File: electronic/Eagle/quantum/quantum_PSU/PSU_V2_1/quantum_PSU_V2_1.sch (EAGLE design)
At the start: 37 parts, among them J1 90814-0204, J2 90814-0204, J3 PF0030_PC, U1 7815, U2 7812, U3 7915, U4 7805, U5 LD1117AV33

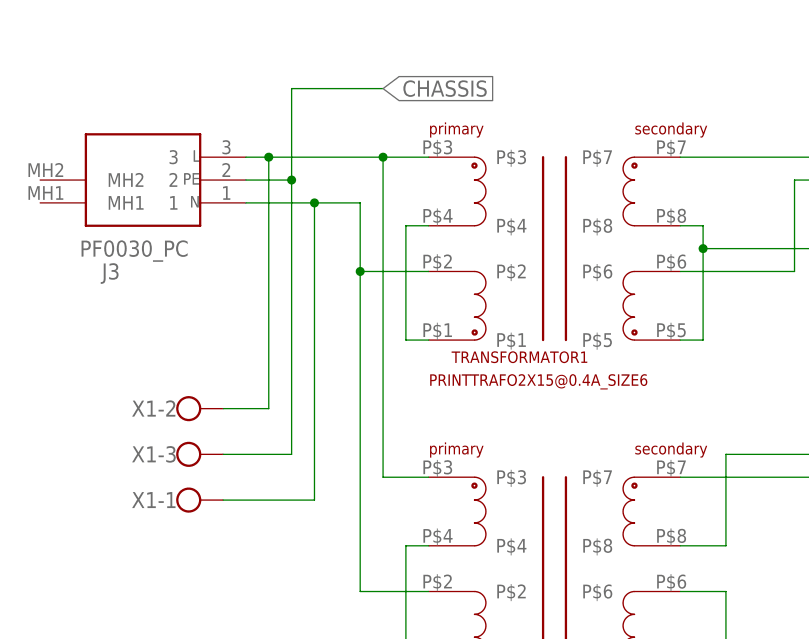
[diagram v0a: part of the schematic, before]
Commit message: several mockups and changes during debugging AnalougeEngine_V5_0. Implemented DSP functionality + rudimental FFT function
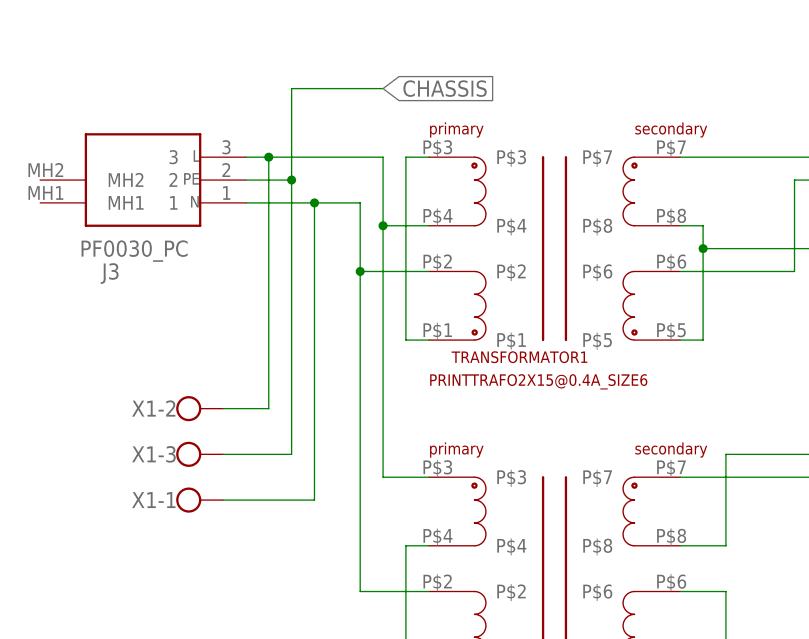
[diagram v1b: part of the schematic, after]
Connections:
- net N$4: now also TRANSFORMATOR1.P$3; no longer TRANSFORMATOR1.P$4
- net N$8: now also TRANSFORMATOR1.P$4; no longer TRANSFORMATOR1.P$3
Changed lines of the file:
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@@
 <layer number="56" name="wert" color="7" fill="1" visible="no" active="no"/>
 <layer number="57" name="tCAD" color="7" fill="1" visible="no" active="no"/>
+<layer number="59" name="tCarbon" color="7" fill="1" visible="no" active="no"/>
+<layer number="60" name="bCarbon" color="7" fill="1" visible="no" active="no"/>
 <layer number="88" name="SimResults" color="9" fill="1" visible="yes" active="yes"/>
 <layer number="89" name="SimProbes" color="9" fill="1" visible="yes" active="yes"/>
@@
 <layer number="112" name="tSilk" color="7" fill="1" visible="no" active="yes"/>
 <layer number="113" name="ReferenceLS" color="7" fill="1" visible="no" active="no"/>
+<layer number="114" name="Badge_Outline" color="11" fill="1" visible="no" active="no"/>
+<layer number="115" name="ReferenceISLANDS" color="7" fill="1" visible="yes" active="yes"/>
 <layer number="116" name="Patch_BOT" color="7" fill="1" visible="yes" active="yes"/>
 <layer number="118" name="Rect_Pads" color="7" fill="1" visible="no" active="no"/>
@@
 <layer number="127" name="_tValues" color="7" fill="1" visible="no" active="yes"/>
 <layer number="128" name="_bValues" color="7" fill="1" visible="no" active="yes"/>
+<layer number="129" name="Mask" color="7" fill="1" visible="yes" active="yes"/>
 <layer number="131" name="tAdjust" color="7" fill="1" visible="no" active="yes"/>
 <layer number="132" name="bAdjust" color="7" fill="1" visible="no" active="yes"/>
@@
 <layer number="223" name="223bmp" color="7" fill="1" visible="yes" active="yes"/>
 <layer number="224" name="224bmp" color="7" fill="1" visible="yes" active="yes"/>
+<layer number="225" name="225bmp" color="7" fill="1" visible="yes" active="yes"/>
+<layer number="226" name="226bmp" color="7" fill="1" visible="yes" active="yes"/>
+<layer number="227" name="227bmp" color="7" fill="1" visible="yes" active="yes"/>
+<layer number="228" name="228bmp" color="7" fill="1" visible="yes" active="yes"/>
+<layer number="229" name="229bmp" color="7" fill="1" visible="yes" active="yes"/>
+<layer number="230" name="230bmp" color="7" fill="1" visible="yes" active="yes"/>
 <layer number="231" name="Eagle3D_PG1" color="7" fill="1" visible="no" active="no"/>
 <layer number="232" name="Eagle3D_PG2" color="7" fill="1" visible="no" active="no"/>
@@
 <layer number="251" name="SMDround" color="7" fill="1" visible="yes" active="yes"/>
 <layer number="254" name="OrgLBR" color="7" fill="1" visible="yes" active="yes"/>
+<layer number="255" name="routoute" color="7" fill="1" visible="yes" active="yes"/>
 </layers>
 <schematic xreflabel="%F%N/%S.%C%R" xrefpart="/%S.%C%R">
@@
 <part name="C3" library="passive components" library_urn="urn:adsk.eagle:library:16365137" deviceset="CAPACITOR_ELECTROLYTIC" device="_16MM-THT" package3d_urn="urn:adsk.eagle:package:1899458/5" value="4700 uF/25 V"/>
 <part name="BR2" library="passive components" library_urn="urn:adsk.eagle:library:16365137" deviceset="BRIDGE_RECTIFIER" device="" package3d_urn="urn:adsk.eagle:package:16388481/3"/>
-<part name="J1" library="electro_mechanical" library_urn="urn:adsk.eagle:library:16388331" deviceset="90814-0204" device="" package3d_urn="urn:adsk.eagle:package:16762552/3"/>
-<part name="J2" library="electro_mechanical" library_urn="urn:adsk.eagle:library:16388331" deviceset="90814-0204" device="" package3d_urn="urn:adsk.eagle:package:16762552/3"/>
+<part name="J1" library="electro_mechanical" library_urn="urn:adsk.eagle:library:16388331" deviceset="90814-0204" device="" package3d_urn="urn:adsk.eagle:package:16762552/4"/>
+<part name="J2" library="electro_mechanical" library_urn="urn:adsk.eagle:library:16388331" deviceset="90814-0204" device="" package3d_urn="urn:adsk.eagle:package:16762552/4"/>
 <part name="J3" library="electro_mechanical" library_urn="urn:adsk.eagle:library:16388331" deviceset="PF0030_PC" device="" package3d_urn="urn:adsk.eagle:package:16991597/2"/>
 <part name="U4" library="passive components" library_urn="urn:adsk.eagle:library:16365137" deviceset="78**" device="_THT" package3d_urn="urn:adsk.eagle:package:1899455/2" value="7805"/>
@@
 <net name="N$8" class="0">
 <segment>
-<pinref part="TRANSFORMATOR1" gate="G$1" pin="P$3"/>
 <pinref part="TRANSFORMATOR2" gate="G$1" pin="P$3"/>
-<wire x1="45.72" y1="154.94" x2="50.8" y2="154.94" width="0.1524" layer="91"/>
 <wire x1="50.8" y1="119.38" x2="45.72" y2="119.38" width="0.1524" layer="91"/>
-<wire x1="45.72" y1="119.38" x2="45.72" y2="154.94" width="0.1524" layer="91"/>
-<junction x="45.72" y="154.94"/>
+<wire x1="45.72" y1="119.38" x2="45.72" y2="147.32" width="0.1524" layer="91"/>
 <pinref part="J3" gate="G$1" pin="3"/>
+<wire x1="45.72" y1="147.32" x2="45.72" y2="154.94" width="0.1524" layer="91"/>
 <wire x1="30.48" y1="154.94" x2="33.02" y2="154.94" width="0.1524" layer="91"/>
 <wire x1="33.02" y1="154.94" x2="45.72" y2="154.94" width="0.1524" layer="91"/>
@@
 <pinref part="X1" gate="-2" pin="KL"/>
 <wire x1="27.94" y1="127" x2="33.02" y2="127" width="0.1524" layer="91"/>
+<pinref part="TRANSFORMATOR1" gate="G$1" pin="P$4"/>
+<wire x1="50.8" y1="147.32" x2="45.72" y2="147.32" width="0.1524" layer="91"/>
+<junction x="45.72" y="147.32"/>
 </segment>
 </net>
@@
 <pinref part="TRANSFORMATOR1" gate="G$1" pin="P$1"/>
 <wire x1="50.8" y1="134.62" x2="48.26" y2="134.62" width="0.1524" layer="91"/>
-<pinref part="TRANSFORMATOR1" gate="G$1" pin="P$4"/>
-<wire x1="48.26" y1="134.62" x2="48.26" y2="147.32" width="0.1524" layer="91"/>
-<wire x1="48.26" y1="147.32" x2="50.8" y2="147.32" width="0.1524" layer="91"/>
-</segment>
-</net>
+<wire x1="48.26" y1="134.62" x2="48.26" y2="154.94" width="0.1524" layer="91"/>
+<pinref part="TRANSFORMATOR1" gate="G$1" pin="P$3"/>
+<wire x1="50.8" y1="154.94" x2="48.26" y2="154.94" width="0.1524" layer="91"/>
+</segment>
+</net>
